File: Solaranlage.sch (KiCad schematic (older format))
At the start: 95 parts, among them J1 Screw_Terminal_01x02, J2 Screw_Terminal_01x02, J3 AVR-JTAG-10, J4 USB_B, J5 USB_B, J6 Screw_Terminal_01x02, Q1 2N3904, SW1 Rotary_Encoder_Switch_Panason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, SW2 SW_SPDT, U1 SC56-11E*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

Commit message: added shift register for GPIO expansion; edited board shape in order to make the display central; designed frontplate; added MCAD assembly to folder 3D;
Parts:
- added D12: K, LED_THT:LED_D3.0mm, symbol Device:LED
- added D13: M, LED_THT:LED_D3.0mm, symbol Device:LED
- added L3: 10uH, Inductor_THT:L_Axial_L9.5mm_D4.0mm_P5.08mm_Vertical_Fastron_SMCC, symbol pspice:INDUCTOR
- added MECH1, MECH2: Socket for NE555 (U10), dummy:void, symbol Solaranlage-rescue:IC-sockets
- added MECH3: Socket for buffer (U11), dummy:void, symbol Solaranlage-rescue:IC-sockets
- added MECH4: Socket shift register (U12), dummy:void, symbol Solaranlage-rescue:IC-sockets
- added MECH5: Socket for ATMega32 (U7), dummy:void, symbol Solaranlage-rescue:IC-sockets
- added R31, R32: 330, Resistor_THT:R_Axial_DIN0204_L3.6mm_D1.6mm_P7.62mm_Horizontal, symbol Device:R
- added U12: 74HC595, Package_DIP:DIP-16_W7.62mm, symbol 74xx:74HC595
- D4: value TD -> D2
- D5: value TD -> D1
- D6: value TD -> TK
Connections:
- net labels added: SR_CLOCK, SR_DATA, SR_LATCH, SR_OE, delta1_ind, delta2_ind, k_ind, mode_ind, temp_dach_ind, temp_keller_ind
- net labels removed: delta1, delta2, temp_dach, temp_keller
- wire segments 462 -> 485
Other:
- note added: "IC socket 16-pin."
- note added: "IC socket 40-pin."
- note added: "IC socket 8-pin."
- moved on the sheet: C18, C22, C7, D1, D10, D11, D3, D4, D5, D6, D7, H1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

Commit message: some cleaning
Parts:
- J4, J5: Ordering (none) -> Conrad: 1883654-62
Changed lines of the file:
@@
 F 2 "Connector_USB:USB_B_Lumberg_2411_02_Horizontal" H 8700 9850 50  0001 C CNN
 F 3 " ~" H 8700 9850 50  0001 C CNN
+F 4 "Conrad: 1883654-62" H 8550 9900 50  0001 C CNN "Ordering"
 	1    8550 9900
 	1    0    0    -1
@@
 F 2 "Connector_USB:USB_B_Lumberg_2411_02_Horizontal" H 1500 13350 50  0001 C CNN
 F 3 " ~" H 1500 13350 50  0001 C CNN
+F 4 "Conrad: 1883654-62" H 1350 13400 50  0001 C CNN "Ordering"
 	1    1350 13400
 	1    0    0    -1

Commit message: rounded up corners of cutout for display in the frontplate
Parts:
- SW1: symbol Solaranlage-rescue:Rotary_Encoder_Switch_Panasonic_EVE-QDBRL416B-Device -> Solaranlage:Rotary_Encoder_Switch_Panasonic_EVE-QDBRL416B-Device
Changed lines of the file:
@@
 SW1
 $Comp
-L Solaranlage-rescue:Rotary_Encoder_Switch_Panasonic_EVE-QDBRL416B-Device SW1
+L Solaranlage:Rotary_Encoder_Switch_Panasonic_EVE-QDBRL416B-Device SW1
 U 1 1 5FAD84A2
 P 19700 3550

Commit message: added optional 1-wire 'interface' (J7); added 3D models to terminal blocks
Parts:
- added J7: Screw_Terminal_01x02, TerminalBlock_MetzConnect:TerminalBlock_MetzConnect_Type171_RT13703HBWC_1x03_P7.50mm_Horizontal, symbol Connector:Screw_Terminal_01x03
- J4, J5: symbol Solaranlage-rescue:USB_B-Connector -> Solaranlage:USB_B-Connector
- MECH1, MECH2, MECH3, MECH4, MECH5: symbol Solaranlage-rescue:IC-sockets -> Solaranlage:IC-sockets
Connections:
- net labels added: ?
- net labels removed: SR_OE
- wire segments 485 -> 492
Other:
- moved on the sheet: D2, R18
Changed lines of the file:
@@
 	8550 10300 8550 10400
 $Comp
-L Solaranlage-rescue:USB_B-Connector J5
+L Solaranlage:USB_B-Connector J5
 U 1 1 5F70CF6B
 P 8550 9900
@@
 	1350 13800 1350 13900
 $Comp
-L Solaranlage-rescue:USB_B-Connector J4
+L Solaranlage:USB_B-Connector J4
 U 1 1 5F70A7FD
 P 1350 13400
@@
 Heart_LED
 Wire Wire Line
-	10650 7050 10650 7200
+	10350 7050 10350 7200
 $Comp
 L Device:R R18
 U 1 1 5FDE6938
-P 10650 6900
-F 0 "R18" H 10720 6946 50  0000 L CNN
-F 1 "560" H 10720 6855 50  0000 L CNN
-F 2 "Resistor_THT:R_Axial_DIN0204_L3.6mm_D1.6mm_P7.62mm_Horizontal" H 10720 6809 50  0001 L CNN
-F 3 "~" H 10650 6900 50  0001 C CNN
-	1    10650 6900
+P 10350 6900
+F 0 "R18" H 10420 6946 50  0000 L CNN
+F 1 "560" H 10420 6855 50  0000 L CNN
+F 2 "Resistor_THT:R_Axial_DIN0204_L3.6mm_D1.6mm_P7.62mm_Horizontal" H 10420 6809 50  0001 L CNN
+F 3 "~" H 10350 6900 50  0001 C CNN
+	1    10350 6900
 	1    0    0    -1
 $EndComp
 Wire Wire Line
-	10650 7500 10650 7700
+	10350 7500 10350 7700
 $Comp
 L power:GND #PWR0106
 U 1 1 5FD2A3D0
-P 10650 7700
-F 0 "#PWR0106" H 10650 7450 50  0001 C CNN
-F 1 "GND" H 10655 7527 50  0000 C CNN
-F 2 "" H 10650 7700 50  0001 C CNN
-F 3 "" H 10650 7700 50  0001 C CNN
-	1    10650 7700
+P 10350 7700
+F 0 "#PWR0106" H 10350 7450 50  0001 C CNN
+F 1 "GND" H 10355 7527 50  0000 C CNN
+F 2 "" H 10350 7700 50  0001 C CNN
+F 3 "" H 10350 7700 50  0001 C CNN
+	1    10350 7700
 	1    0    0    -1
 $EndComp
@@
 L Device:LED D2
 U 1 1 5FCF85FA
-P 10650 7350
-F 0 "D2" V 10650 7450 50  0000 C CNN
-F 1 "LED_gruen" V 10550 7550 50  0000 C CNN
-F 2 "LED_THT:LED_D5.0mm" H 10650 7350 50  0001 C CNN
-F 3 "~" H 10650 7350 50  0001 C CNN
-	1    10650 7350
+P 10350 7350
+F 0 "D2" V 10350 7450 50  0000 C CNN
+F 1 "LED_gruen" V 10250 7550 50  0000 C CNN
+F 2 "LED_THT:LED_D5.0mm" H 10350 7350 50  0001 C CNN
+F 3 "~" H 10350 7350 50  0001 C CNN
+	1    10350 7350
 	0    -1   -1   0
 $EndComp
@@
 $EndComp
 Wire Wire Line
-	10650 6650 10650 6750
+	10350 6650 10350 6750
 Wire Wire Line
 	14000 4050 14000 3050
@@
 	14450 3850 14450 4200
 Wire Wire Line
-	10650 6650 12700 6650
+	10350 6650 12700 6650
 Wire Wire Line
 	12700 3550 5450 3550
@@
 $EndComp
 Wire Wire Line
-	11250 6850 12700 6850
-Text GLabel 11250 6850 0    50   Output ~ 0
+	11550 6850 12700 6850
+Text GLabel 11550 6850 0    50   Output ~ 0
 PWM
 Text GLabel 9950 12850 2    50   Input ~ 0
@@
 F 1 "74HC595" H 19950 9450 50  0000 C CNN
 F 2 "Package_DIP:DIP-16_W7.62mm" H 20200 10150 50  0001 C CNN
-F 3 "http://www.ti.com/lit/ds/symlink/sn74hc595.pdf" H 20200 10150 50  0001 C CNN
+F 3 "${KIPRJMOD}\\datasheets\\74HC595.pdf" H 20200 10150 50  0001 C CNN
 F 4 "Reichel: 74HC 595" H 20200 10150 50  0001 C CNN "Ordering"
 	1    20200 10150
@@
 Text GLabel 19500 10250 0    50   Input ~ 0
 SR_LATCH
-Text GLabel 19500 10350 0    50   Input ~ 0
-SR_OE
-Wire Wire Line
-	19800 10350 19500 10350
 Wire Wire Line
 	19800 9750 19500 9750
@@
 SR_LATCH
 Wire Wire Line
-	12700 6750 11550 6750
+	12700 6750 11250 6750
 Text Label 12150 6750 0    50   ~ 0
-SR_OE
-Text GLabel 11550 6750 0    50   Output ~ 0
-SR_OE
+?
 Connection ~ 11150 9600
 Wire Wire Line
@@
 $EndComp
 $Comp
-L Solaranlage-rescue:IC-sockets MECH1
+L Solaranlage:IC-sockets MECH1
 U 1 1 63E81666
 P 13800 13200
@@
 $EndComp
 $Comp
-L Solaranlage-rescue:IC-sockets MECH2
+L Solaranlage:IC-sockets MECH2
 U 1 1 63E83912
 P 13800 13600
@@
 $EndComp
 $Comp
-L Solaranlage-rescue:IC-sockets MECH3
+L Solaranlage:IC-sockets MECH3
 U 1 1 6405078D
 P 15200 13200
@@
 $EndComp
 $Comp
-L Solaranlage-rescue:IC-sockets MECH4
+L Solaranlage:IC-sockets MECH4
 U 1 1 640D3CA4
 P 15200 13600
@@
 $EndComp
 $Comp
-L Solaranlage-rescue:IC-sockets MECH5
+L Solaranlage:IC-sockets MECH5
 U 1 1 641D9EF1
 P 16650 13200
@@
 	1    0    0    -1
 $EndComp
+Wire Wire Line
+	19800 10350 18950 10350
+Wire Wire Line
+	18950 10350 18950 11150
+$Comp
+L power:GND #PWR0110
+U 1 1 604ADA4B
+P 18950 11150
+F 0 "#PWR0110" H 18950 10900 50  0001 C CNN
+F 1 "GND" H 18955 10977 50  0000 C CNN
+F 2 "" H 18950 11150 50  0001 C CNN
+F 3 "" H 18950 11150 50  0001 C CNN
+	1    18950 11150
+	1    0    0    -1
+$EndComp
+$Comp
+L Connector:Screw_Terminal_01x03 J7
+U 1 1 6050B64A
+P 10750 7350
+F 0 "J7" H 10750 7150 50  0000 C CNN
+F 1 "Screw_Terminal_01x02" H 11100 7450 50  0001 C CNN
+F 2 "TerminalBlock_MetzConnect:TerminalBlock_MetzConnect_Type171_RT13703HBWC_1x03_P7.50mm_Horizontal" H 10750 7350 50  0001 C CNN
+F 3 "~" H 10750 7350 50  0001 C CNN
+	1    10750 7350
+	-1   0    0    1
+$EndComp
+Wire Wire Line
+	10950 7350 11250 7350
+Wire Wire Line
+	11250 7350 11250 6750
+Wire Wire Line
+	10950 7450 11000 7450
+Wire Wire Line
+	11000 7450 11000 7750
+$Comp
+L power:GND #PWR0119
+U 1 1 607A2F9A
+P 11000 7750
+F 0 "#PWR0119" H 11000 7500 50  0001 C CNN
+F 1 "GND" H 11005 7577 50  0000 C CNN
+F 2 "" H 11000 7750 50  0001 C CNN
+F 3 "" H 11000 7750 50  0001 C CNN
+	1    11000 7750
+	1    0    0    -1
+$EndComp
+Wire Wire Line
+	10950 7250 11000 7250
+Wire Wire Line
+	11000 7250 11000 7000
+$Comp
+L power:+5V #PWR0120
+U 1 1 608F3E8E
+P 11000 7000
+F 0 "#PWR0120" H 11000 6850 50  0001 C CNN
+F 1 "+5V" H 11015 7173 50  0000 C CNN
+F 2 "" H 11000 7000 50  0001 C CNN
+F 3 "" H 11000 7000 50  0001 C CNN
+	1    11000 7000
+	1    0    0    -1
+$EndComp

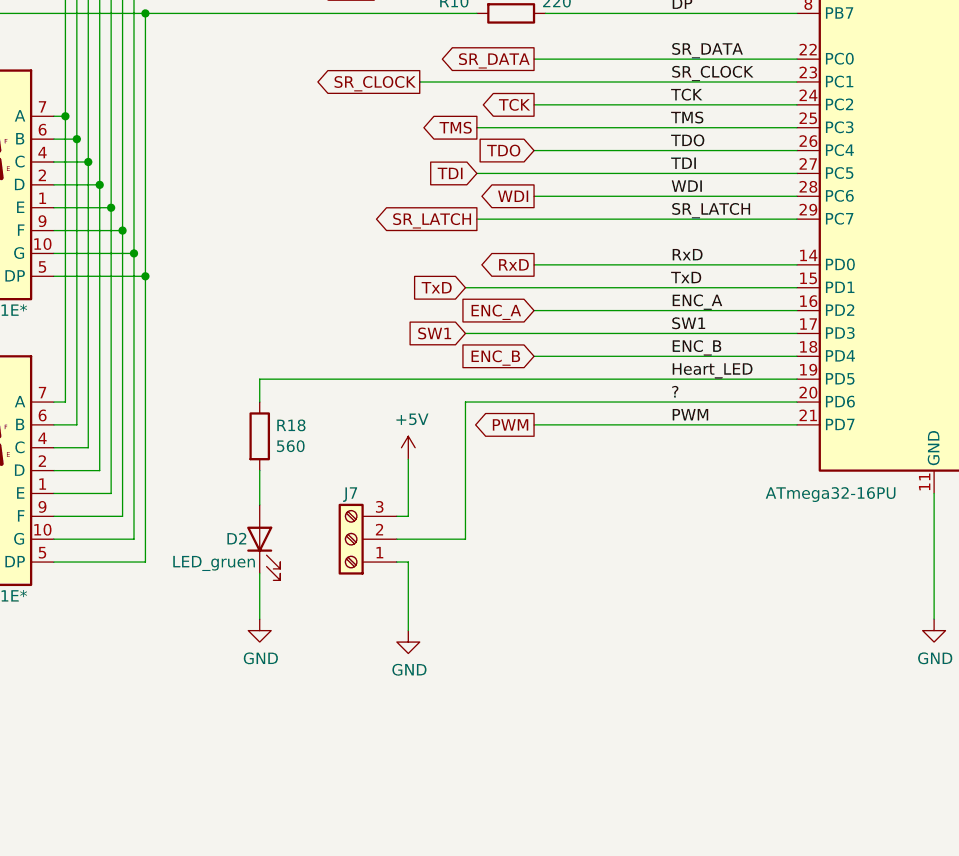
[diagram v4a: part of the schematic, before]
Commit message: added input protection and filtering to 1-wire input
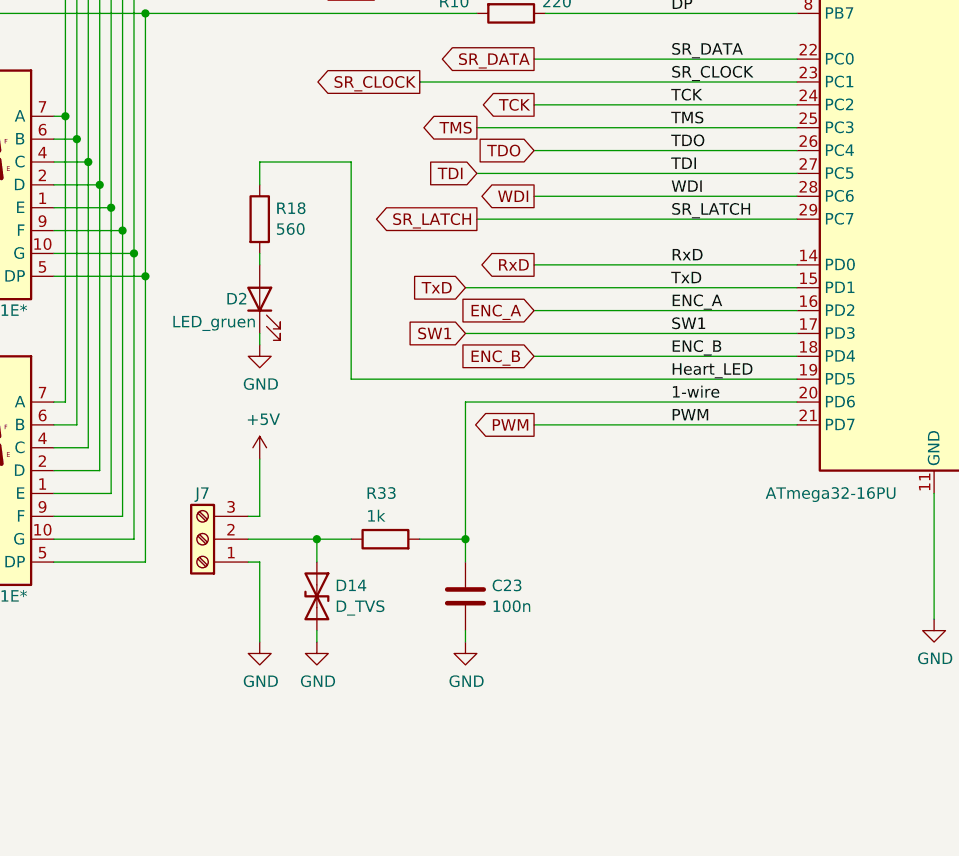
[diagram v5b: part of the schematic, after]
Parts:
- added C23: 100n, Capacitor_THT:C_Disc_D4.7mm_W2.5mm_P5.00mm, symbol Device:C
- added D14: D_TVS, Diode_THT:D_DO-201_P3.81mm_Vertical_KathodeUp, symbol Device:D_TVS
- added R33: 1k, Resistor_THT:R_Axial_DIN0204_L3.6mm_D1.6mm_P7.62mm_Horizontal, symbol Device:R
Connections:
- net GND: now also C23.2, D14.2 (A2)
- net ?: no longer names the net of J7.2 (Pin_2)
- net ?: now also D14.1 (A1), R33.1; no longer U7.20 (PD6)
- new net 1-wire: C23.1, R33.2, U7.20 (PD6)
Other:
- moved on the sheet: D2, J7, R18
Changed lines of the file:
@@
 Heart_LED
 Wire Wire Line
-	10350 7050 10350 7200
+	10350 6100 10350 6150
 $Comp
 L Device:R R18
 U 1 1 5FDE6938
-P 10350 6900
-F 0 "R18" H 10420 6946 50  0000 L CNN
-F 1 "560" H 10420 6855 50  0000 L CNN
-F 2 "Resistor_THT:R_Axial_DIN0204_L3.6mm_D1.6mm_P7.62mm_Horizontal" H 10420 6809 50  0001 L CNN
-F 3 "~" H 10350 6900 50  0001 C CNN
-	1    10350 6900
-	1    0    0    -1
-$EndComp
-Wire Wire Line
-	10350 7500 10350 7700
+P 10350 5950
+F 0 "R18" H 10420 5996 50  0000 L CNN
+F 1 "560" H 10420 5905 50  0000 L CNN
+F 2 "Resistor_THT:R_Axial_DIN0204_L3.6mm_D1.6mm_P7.62mm_Horizontal" H 10420 5859 50  0001 L CNN
+F 3 "~" H 10350 5950 50  0001 C CNN
+	1    10350 5950
+	1    0    0    -1
+$EndComp
+Wire Wire Line
+	10350 6450 10350 6500
 $Comp
 L power:GND #PWR0106
 U 1 1 5FD2A3D0
-P 10350 7700
-F 0 "#PWR0106" H 10350 7450 50  0001 C CNN
-F 1 "GND" H 10355 7527 50  0000 C CNN
-F 2 "" H 10350 7700 50  0001 C CNN
-F 3 "" H 10350 7700 50  0001 C CNN
-	1    10350 7700
+P 10350 6500
+F 0 "#PWR0106" H 10350 6250 50  0001 C CNN
+F 1 "GND" H 10355 6327 50  0000 C CNN
+F 2 "" H 10350 6500 50  0001 C CNN
+F 3 "" H 10350 6500 50  0001 C CNN
+	1    10350 6500
 	1    0    0    -1
 $EndComp
@@
 L Device:LED D2
 U 1 1 5FCF85FA
-P 10350 7350
-F 0 "D2" V 10350 7450 50  0000 C CNN
-F 1 "LED_gruen" V 10250 7550 50  0000 C CNN
-F 2 "LED_THT:LED_D5.0mm" H 10350 7350 50  0001 C CNN
-F 3 "~" H 10350 7350 50  0001 C CNN
-	1    10350 7350
+P 10350 6300
+F 0 "D2" V 10350 6400 50  0000 C CNN
+F 1 "LED_gruen" V 10250 6500 50  0000 C CNN
+F 2 "LED_THT:LED_D5.0mm" H 10350 6300 50  0001 C CNN
+F 3 "~" H 10350 6300 50  0001 C CNN
+	1    10350 6300
 	0    -1   -1   0
 $EndComp
@@
 $EndComp
 Wire Wire Line
-	10350 6650 10350 6750
+	10350 5700 10350 5800
 Wire Wire Line
 	14000 4050 14000 3050
@@
 Wire Wire Line
 	14450 3850 14450 4200
-Wire Wire Line
-	10350 6650 12700 6650
 Wire Wire Line
 	12700 3550 5450 3550
@@
 	12700 6750 11250 6750
 Text Label 12150 6750 0    50   ~ 0
-?
+1-wire
 Connection ~ 11150 9600
 Wire Wire Line
@@
 L Connector:Screw_Terminal_01x03 J7
 U 1 1 6050B64A
-P 10750 7350
-F 0 "J7" H 10750 7150 50  0000 C CNN
-F 1 "Screw_Terminal_01x02" H 11100 7450 50  0001 C CNN
-F 2 "TerminalBlock_MetzConnect:TerminalBlock_MetzConnect_Type171_RT13703HBWC_1x03_P7.50mm_Horizontal" H 10750 7350 50  0001 C CNN
-F 3 "~" H 10750 7350 50  0001 C CNN
-	1    10750 7350
+P 10100 7350
+F 0 "J7" H 10100 7150 50  0000 C CNN
+F 1 "Screw_Terminal_01x02" H 10450 7450 50  0001 C CNN
+F 2 "TerminalBlock_MetzConnect:TerminalBlock_MetzConnect_Type171_RT13703HBWC_1x03_P7.50mm_Horizontal" H 10100 7350 50  0001 C CNN
+F 3 "~" H 10100 7350 50  0001 C CNN
+	1    10100 7350
 	-1   0    0    1
 $EndComp
 Wire Wire Line
-	10950 7350 11250 7350
-Wire Wire Line
-	11250 7350 11250 6750
-Wire Wire Line
-	10950 7450 11000 7450
-Wire Wire Line
-	11000 7450 11000 7750
+	10300 7350 10600 7350
+Wire Wire Line
+	10300 7450 10350 7450
+Wire Wire Line
+	10350 7450 10350 7800
 $Comp
 L power:GND #PWR0119
 U 1 1 607A2F9A
-P 11000 7750
-F 0 "#PWR0119" H 11000 7500 50  0001 C CNN
-F 1 "GND" H 11005 7577 50  0000 C CNN
-F 2 "" H 11000 7750 50  0001 C CNN
-F 3 "" H 11000 7750 50  0001 C CNN
-	1    11000 7750
-	1    0    0    -1
-$EndComp
-Wire Wire Line
-	10950 7250 11000 7250
-Wire Wire Line
-	11000 7250 11000 7000
+P 10350 7800
+F 0 "#PWR0119" H 10350 7550 50  0001 C CNN
+F 1 "GND" H 10355 7627 50  0000 C CNN
+F 2 "" H 10350 7800 50  0001 C CNN
+F 3 "" H 10350 7800 50  0001 C CNN
+	1    10350 7800
+	1    0    0    -1
+$EndComp
+Wire Wire Line
+	10300 7250 10350 7250
+Wire Wire Line
+	10350 7250 10350 7000
 $Comp
 L power:+5V #PWR0120
 U 1 1 608F3E8E
-P 11000 7000
-F 0 "#PWR0120" H 11000 6850 50  0001 C CNN
-F 1 "+5V" H 11015 7173 50  0000 C CNN
-F 2 "" H 11000 7000 50  0001 C CNN
-F 3 "" H 11000 7000 50  0001 C CNN
-	1    11000 7000
-	1    0    0    -1
+P 10350 7000
+F 0 "#PWR0120" H 10350 6850 50  0001 C CNN
+F 1 "+5V" H 10365 7173 50  0000 C CNN
+F 2 "" H 10350 7000 50  0001 C CNN
+F 3 "" H 10350 7000 50  0001 C CNN
+	1    10350 7000
+	1    0    0    -1
+$EndComp
+$Comp
+L Device:D_TVS D14
+U 1 1 611E8379
+P 10600 7600
+F 0 "D14" V 10554 7680 50  0000 L CNN
+F 1 "D_TVS" V 10645 7680 50  0000 L CNN
+F 2 "Diode_THT:D_DO-201_P3.81mm_Vertical_KathodeUp" H 10600 7600 50  0001 C CNN
+F 3 "${KIPRJMOD}\\datasheets\\TVS_P6KE6.8A.pdf" H 10600 7600 50  0001 C CNN
+F 4 "Conrad: 140823 - 62" V 10600 7600 50  0001 C CNN "Ordering"
+	1    10600 7600
+	0    1    1    0
+$EndComp
+$Comp
+L power:GND #PWR057
+U 1 1 611E8393
+P 10600 7800
+F 0 "#PWR057" H 10600 7550 50  0001 C CNN
+F 1 "GND" H 10605 7627 50  0000 C CNN
+F 2 "" H 10600 7800 50  0001 C CNN
+F 3 "" H 10600 7800 50  0001 C CNN
+	1    10600 7800
+	1    0    0    -1
+$EndComp
+Wire Wire Line
+	10600 7350 10600 7450
+Wire Wire Line
+	10600 7750 10600 7800
+Wire Wire Line
+	10350 5700 10750 5700
+Wire Wire Line
+	10750 5700 10750 6650
+Wire Wire Line
+	10750 6650 12700 6650
+Connection ~ 10600 7350
+Wire Wire Line
+	10600 7350 10750 7350
+Wire Wire Line
+	11250 7750 11250 7800
+$Comp
+L power:GND #PWR058
+U 1 1 615F46C0
+P 11250 7800
+F 0 "#PWR058" H 11250 7550 50  0001 C CNN
+F 1 "GND" H 11255 7627 50  0000 C CNN
+F 2 "" H 11250 7800 50  0001 C CNN
+F 3 "" H 11250 7800 50  0001 C CNN
+	1    11250 7800
+	1    0    0    -1
+$EndComp
+$Comp
+L Device:C C23
+U 1 1 615AF6B9
+P 11250 7600
+F 0 "C23" H 11365 7646 50  0000 L CNN
+F 1 "100n" H 11365 7555 50  0000 L CNN
+F 2 "Capacitor_THT:C_Disc_D4.7mm_W2.5mm_P5.00mm" H 11288 7450 50  0001 C CNN
+F 3 "~" H 11250 7600 50  0001 C CNN
+	1    11250 7600
+	1    0    0    -1
+$EndComp
+Wire Wire Line
+	11250 7350 11250 7450
+Wire Wire Line
+	11250 7350 11250 6750
+Connection ~ 11250 7350
+Wire Wire Line
+	11050 7350 11250 7350
+$Comp
+L Device:R R33
+U 1 1 6156A24B
+P 10900 7350
+F 0 "R33" V 11100 7300 50  0000 L CNN
+F 1 "1k" V 11000 7350 50  0000 L CNN
+F 2 "Resistor_THT:R_Axial_DIN0204_L3.6mm_D1.6mm_P7.62mm_Horizontal" H 10970 7259 50  0001 L CNN
+F 3 "~" H 10900 7350 50  0001 C CNN
+	1    10900 7350
+	0    -1   -1   0
 $EndComp
 $EndSCHEMATC

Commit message: -
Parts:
- removed C23: 100n, Capacitor_THT:C_Disc_D4.7mm_W2.5mm_P5.00mm, symbol Device:C
- removed U11: 74LS125, Package_DIP:DIP-14_W7.62mm, symbol 74xx:74LS125
- added F1: Fuse, fuse:5x20mm, symbol Device:Fuse
- added R34: 10k, Resistor_THT:R_Axial_DIN0204_L3.6mm_D1.6mm_P7.62mm_Horizontal, symbol Device:R
- added U11: 74LS126, Package_DIP:DIP-14_W7.62mm, symbol 74xx:74LS126
- R33: value 1k -> 4k7
- SW2: value SW_SPDT -> 100SP1T1B4M2QE
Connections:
- net +5V: now also R33.2, R34.1, U11.14 (VCC)
- net 1-wire: now also D14.1 (A1), J7.2 (Pin_2), R33.1; no longer R33.2
- net GND: now also U11.7 (GND)
- net PWM: now also U11.12, U11.2, U11.5, U11.9
- net PWM2: now also R34.2
- net \RST: now also U11.1, U11.10, U11.13, U11.4
- net at D10.1 (A1), J5.1 (VBUS): now also F1.2; no longer SW2.2 (B)
- net at R12.1: now also U11.3
- net at R13.1: now also U11.6
- net at R19.1: now also U11.8
- net at R21.1: now also U11.11
- new net: F1.1, SW2.2 (B)
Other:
- moved on the sheet: D10, D14, J7, R33
